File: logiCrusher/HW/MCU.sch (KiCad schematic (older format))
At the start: 13 parts, among them J2 Conn_02x05_Odd_Even, J5 Conn_01x10, J6 Conn_01x10, SW1 SW_Push, U4 STM32F373CCTx

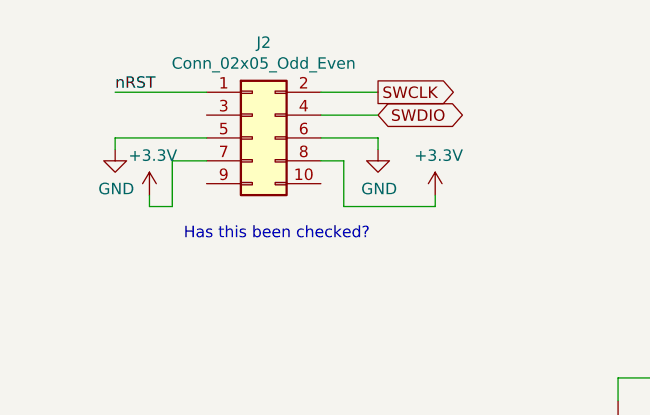
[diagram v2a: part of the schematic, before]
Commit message: Worked on the layout for the logicrusher
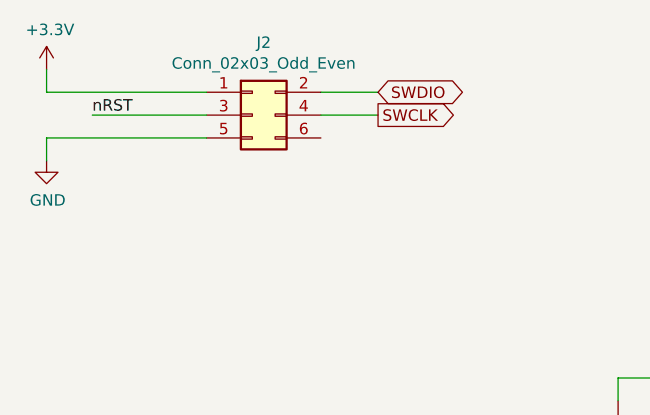
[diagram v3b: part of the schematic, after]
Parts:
- removed J2: Conn_02x05_Odd_Even, symbol Connector_Generic:Conn_02x05_Odd_Even
- added J2: Conn_02x03_Odd_Even, Connector_PinHeader_2.54mm:PinHeader_2x03_P2.54mm_Vertical, symbol Connector_Generic:Conn_02x03_Odd_Even
- J5, J6: footprint (none) -> Connector_PinHeader_2.54mm:PinHeader_1x10_P2.54mm_Vertical
- SW1: footprint (none) -> Button_Switch_THT:SW_Tactile_Straight_KSL0Axx1LFTR
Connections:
- net +3V3: now also J2.1 (Pin_1)
- net GND: now also J2.5 (Pin_5)
- net SWCLK: now also J2.4 (Pin_4)
- net SWDIO: now also J2.2 (Pin_2)
- net nRST: now also J2.3 (Pin_3)
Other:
- note removed: "Has this been checked?"
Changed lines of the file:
@@
 F 0 "SW1" V 3396 2802 50  0000 R CNN
 F 1 "SW_Push" V 3305 2802 50  0000 R CNN
-F 2 "" H 3350 3050 50  0001 C CNN
+F 2 "Button_Switch_THT:SW_Tactile_Straight_KSL0Axx1LFTR" H 3350 3050 50  0001 C CNN
 F 3 "" H 3350 3050 50  0001 C CNN
 	1    3350 2850
@@
 F 0 "J5" H 7830 4642 50  0000 L CNN
 F 1 "Conn_01x10" H 7830 4551 50  0000 L CNN
-F 2 "" H 7750 4650 50  0001 C CNN
+F 2 "Connector_PinHeader_2.54mm:PinHeader_1x10_P2.54mm_Vertical" H 7750 4650 50  0001 C CNN
 F 3 "~" H 7750 4650 50  0001 C CNN
 	1    7750 4650
@@
 F 0 "J6" V 8400 2450 50  0000 L CNN
 F 1 "Conn_01x10" V 8500 2450 50  0000 L CNN
-F 2 "" H 8300 2950 50  0001 C CNN
+F 2 "Connector_PinHeader_2.54mm:PinHeader_1x10_P2.54mm_Vertical" H 8300 2950 50  0001 C CNN
 F 3 "~" H 8300 2950 50  0001 C CNN
 	1    8300 2950
@@
 Text Label 6850 2850 0    50   ~ 0
 ADC3
-Text GLabel 2300 1300 2    50   Output ~ 0
+Text GLabel 2300 1400 2    50   Output ~ 0
 SWCLK
-Text GLabel 2300 1400 2    50   BiDi ~ 0
+Text GLabel 2300 1300 2    50   BiDi ~ 0
 SWDIO
-Text Label 1150 1300 0    50   ~ 0
+Text Label 1050 1400 0    50   ~ 0
 nRST
-$Comp
-L Connector_Generic:Conn_02x05_Odd_Even J?
-U 1 1 5CBA4E93
-P 1750 1500
-AR Path="/5CBA4E93" Ref="J?"  Part="1"
-AR Path="/5CB08311/5CBA4E93" Ref="J2"  Part="1"
-F 0 "J2" H 1800 1917 50  0000 C CNN
-F 1 "Conn_02x05_Odd_Even" H 1800 1826 50  0000 C CNN
-F 2 "" H 1750 1500 50  0001 C CNN
-F 3 "~" H 1750 1500 50  0001 C CNN
-	1    1750 1500
-	1    0    0    -1
-$EndComp
-Wire Wire Line
-	1150 1300 1550 1300
-Wire Wire Line
-	1550 1500 1150 1500
-Wire Wire Line
-	1150 1500 1150 1550
-$Comp
-L power:GND #PWR?
-U 1 1 5CBA4E9D
-P 1150 1550
-AR Path="/5CBA4E9D" Ref="#PWR?"  Part="1"
-AR Path="/5CB08311/5CBA4E9D" Ref="#PWR019"  Part="1"
-F 0 "#PWR019" H 1150 1300 50  0001 C CNN
-F 1 "GND" H 1155 1377 50  0000 C CNN
-F 2 "" H 1150 1550 50  0001 C CNN
-F 3 "" H 1150 1550 50  0001 C CNN
-	1    1150 1550
-	1    0    0    -1
-$EndComp
-$Comp
-L power:GND #PWR?
-U 1 1 5CBA4EA3
-P 2300 1550
-AR Path="/5CBA4EA3" Ref="#PWR?"  Part="1"
-AR Path="/5CB08311/5CBA4EA3" Ref="#PWR022"  Part="1"
-F 0 "#PWR022" H 2300 1300 50  0001 C CNN
-F 1 "GND" H 2305 1377 50  0000 C CNN
-F 2 "" H 2300 1550 50  0001 C CNN
-F 3 "" H 2300 1550 50  0001 C CNN
-	1    2300 1550
-	1    0    0    -1
-$EndComp
+Wire Wire Line
+	850  1300 1550 1300
 Wire Wire Line
 	2050 1300 2300 1300
 Wire Wire Line
 	2050 1400 2300 1400
-Wire Wire Line
-	2050 1500 2300 1500
-Wire Wire Line
-	2300 1500 2300 1550
-$Comp
-L power:+3.3V #PWR?
-U 1 1 5CBA4EAD
-P 1300 1750
-AR Path="/5CBA4EAD" Ref="#PWR?"  Part="1"
-AR Path="/5CB08311/5CBA4EAD" Ref="#PWR021"  Part="1"
-F 0 "#PWR021" H 1300 1600 50  0001 C CNN
-F 1 "+3.3V" H 1315 1923 50  0000 C CNN
-F 2 "" H 1300 1750 50  0001 C CNN
-F 3 "" H 1300 1750 50  0001 C CNN
-	1    1300 1750
-	1    0    0    -1
-$EndComp
-Wire Wire Line
-	1300 1750 1300 1800
-Wire Wire Line
-	1300 1800 1400 1800
-Wire Wire Line
-	1400 1800 1400 1600
-Wire Wire Line
-	1400 1600 1550 1600
-Wire Wire Line
-	2050 1600 2150 1600
-Wire Wire Line
-	2150 1600 2150 1800
-Wire Wire Line
-	2150 1800 2550 1800
-Wire Wire Line
-	2550 1800 2550 1750
-$Comp
-L power:+3.3V #PWR?
-U 1 1 5CBA4EBB
-P 2550 1750
-AR Path="/5CBA4EBB" Ref="#PWR?"  Part="1"
-AR Path="/5CB08311/5CBA4EBB" Ref="#PWR023"  Part="1"
-F 0 "#PWR023" H 2550 1600 50  0001 C CNN
-F 1 "+3.3V" H 2565 1923 50  0000 C CNN
-F 2 "" H 2550 1750 50  0001 C CNN
-F 3 "" H 2550 1750 50  0001 C CNN
-	1    2550 1750
-	1    0    0    -1
-$EndComp
 Text HLabel 6850 4350 2    50   Input ~ 0
 Vin
@@
 Wire Wire Line
 	7550 2400 7550 2850
-Text Notes 1450 1950 0    50   ~ 0
-Has this been checked?
 Wire Wire Line
 	6650 2550 7250 2550
@@
 Wire Wire Line
 	3900 3300 4450 3300
+$Comp
+L power:+3.3V #PWR?
+U 1 1 5CC2437C
+P 850 1200
+AR Path="/5CC2437C" Ref="#PWR?"  Part="1"
+AR Path="/5CB08311/5CC2437C" Ref="#PWR0103"  Part="1"
+F 0 "#PWR0103" H 850 1050 50  0001 C CNN
+F 1 "+3.3V" H 865 1373 50  0000 C CNN
+F 2 "" H 850 1200 50  0001 C CNN
+F 3 "" H 850 1200 50  0001 C CNN
+	1    850  1200
+	1    0    0    -1
+$EndComp
+Wire Wire Line
+	1050 1400 1550 1400
+Wire Wire Line
+	1550 1500 850  1500
+Wire Wire Line
+	850  1500 850  1600
+$Comp
+L power:GND #PWR?
+U 1 1 5CC2EAFE
+P 850 1600
+AR Path="/5CC2EAFE" Ref="#PWR?"  Part="1"
+AR Path="/5CB08311/5CC2EAFE" Ref="#PWR0104"  Part="1"
+F 0 "#PWR0104" H 850 1350 50  0001 C CNN
+F 1 "GND" H 855 1427 50  0000 C CNN
+F 2 "" H 850 1600 50  0001 C CNN
+F 3 "" H 850 1600 50  0001 C CNN
+	1    850  1600
+	1    0    0    -1
+$EndComp
+Wire Wire Line
+	850  1300 850  1200
+$Comp
+L Connector_Generic:Conn_02x03_Odd_Even J2
+U 1 1 5CC38546
+P 1750 1400
+F 0 "J2" H 1800 1717 50  0000 C CNN
+F 1 "Conn_02x03_Odd_Even" H 1800 1626 50  0000 C CNN
+F 2 "Connector_PinHeader_2.54mm:PinHeader_2x03_P2.54mm_Vertical" H 1750 1400 50  0001 C CNN
+F 3 "~" H 1750 1400 50  0001 C CNN
+	1    1750 1400
+	1    0    0    -1
+$EndComp
 $EndSCHEMATC

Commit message: Spend a lot of time working on the logicCrusher HW
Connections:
- net D0: now reaches J5.1 (Pin_1), U4.18 (PB0)
- net D1: now reaches J5.2 (Pin_2), U4.19 (PB1)
- net D2: now reaches J5.3 (Pin_3), U4.39 (PB3)
- net D3: now reaches J5.4 (Pin_4), U4.40 (PB4)
- net D4: now reaches J5.5 (Pin_5), U4.41 (PB5)
- net D5: now reaches J5.6 (Pin_6), U4.42 (PB6)
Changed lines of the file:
@@
 $EndComp
 Wire Wire Line
-	6650 4450 7550 4450
-Wire Wire Line
-	6650 4550 7550 4550
-Wire Wire Line
-	6650 4650 7550 4650
-Wire Wire Line
-	7550 4750 6650 4750
+	6650 4450 7400 4450
+Wire Wire Line
+	6650 4550 7500 4550
+Wire Wire Line
+	6650 4650 7050 4650
+Wire Wire Line
+	7550 4750 7150 4750
 Wire Wire Line
 	6650 4850 7550 4850
@@
 	7100 4250 7100 4350
 Wire Wire Line
-	7100 4350 7550 4350
+	7100 4350 7300 4350
 Wire Wire Line
 	6650 4150 7200 4150
 Wire Wire Line
 	7200 4150 7200 4250
-Wire Wire Line
-	7200 4250 7550 4250
 Wire Wire Line
 	7550 5150 6650 5150
@@
 	1    0    0    -1
 $EndComp
+Text HLabel 7200 4100 1    50   Output ~ 0
+D0
+Text HLabel 7300 4100 1    50   Output ~ 0
+D1
+Text HLabel 7400 4100 1    50   Output ~ 0
+D2
+Text HLabel 7500 4100 1    50   Output ~ 0
+D3
+Wire Wire Line
+	7200 4100 7200 4150
+Wire Wire Line
+	7200 4250 7550 4250
+Wire Wire Line
+	7300 4100 7300 4350
+Connection ~ 7300 4350
+Wire Wire Line
+	7300 4350 7550 4350
+Wire Wire Line
+	7400 4100 7400 4450
+Connection ~ 7400 4450
+Wire Wire Line
+	7400 4450 7550 4450
+Connection ~ 7500 4550
+Wire Wire Line
+	7500 4550 7550 4550
+Text HLabel 7050 5250 3    50   Input ~ 0
+D4
+Text HLabel 7150 5250 3    50   Input ~ 0
+D5
+Wire Wire Line
+	7050 5250 7050 4650
+Connection ~ 7050 4650
+Wire Wire Line
+	7050 4650 7550 4650
+Wire Wire Line
+	7150 5250 7150 4750
+Connection ~ 7150 4750
+Wire Wire Line
+	7150 4750 6650 4750
+Connection ~ 7200 4150
+Wire Wire Line
+	7500 4100 7500 4550
 $EndSCHEMATC

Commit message: Made fabrication files
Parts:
- removed SW1: SW_Push, Button_Switch_THT:SW_Tactile_Straight_KSL0Axx1LFTR, symbol Switch:SW_Push
- added SW1: TL1105SPF250Q, Eurocad:TL1105SPF250Q, symbol eurocad:TL1105SPF250Q
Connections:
- net GND: now also SW1.3
- net nRST: now also SW1.1, SW1.2
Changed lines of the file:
@@
 Text GLabel 6800 3950 2    50   BiDi ~ 0
 SWDIO
-$Comp
-L Switch:SW_Push SW?
-U 1 1 5CB1AF99
-P 3350 2850
-AR Path="/5CB1AF99" Ref="SW?"  Part="1"
-AR Path="/5CB08311/5CB1AF99" Ref="SW1"  Part="1"
-F 0 "SW1" V 3396 2802 50  0000 R CNN
-F 1 "SW_Push" V 3305 2802 50  0000 R CNN
-F 2 "Button_Switch_THT:SW_Tactile_Straight_KSL0Axx1LFTR" H 3350 3050 50  0001 C CNN
-F 3 "" H 3350 3050 50  0001 C CNN
-	1    3350 2850
-	0    -1   -1   0
-$EndComp
-Wire Wire Line
-	3350 2650 3350 2550
 Wire Wire Line
 	3350 3050 3350 3100
@@
 Wire Wire Line
 	3800 3050 3350 3050
-Connection ~ 3350 3050
 Wire Wire Line
 	5250 2750 4750 2750
@@
 	0    1    1    0
 $EndComp
-Wire Wire Line
-	3350 2550 3800 2550
 Connection ~ 3800 2550
 Wire Wire Line
@@
 Wire Wire Line
 	7500 4100 7500 4550
+$Comp
+L eurocad:TL1105SPF250Q SW1
+U 1 1 5CC32E6D
+P 2500 2900
+F 0 "SW1" V 2454 3228 50  0000 L CNN
+F 1 "TL1105SPF250Q" V 2545 3228 50  0000 L CNN
+F 2 "Eurocad:TL1105SPF250Q" H 2500 2900 50  0001 C CNN
+F 3 "" H 2500 2900 50  0000 C CNN
+	1    2500 2900
+	0    1    1    0
+$EndComp
+Wire Wire Line
+	2300 2600 2300 2550
+Wire Wire Line
+	2300 2550 2700 2550
+Wire Wire Line
+	2700 2600 2700 2550
+Connection ~ 2700 2550
+Wire Wire Line
+	2700 2550 3800 2550
+Wire Wire Line
+	2300 3200 2300 3300
+Wire Wire Line
+	2300 3300 2500 3300
+Wire Wire Line
+	2700 3300 2700 3200
+$Comp
+L power:GND #PWR?
+U 1 1 5CC4367C
+P 2500 3400
+AR Path="/5CC4367C" Ref="#PWR?"  Part="1"
+AR Path="/5CB08311/5CC4367C" Ref="#PWR0105"  Part="1"
+F 0 "#PWR0105" H 2500 3150 50  0001 C CNN
+F 1 "GND" H 2505 3227 50  0000 C CNN
+F 2 "" H 2500 3400 50  0001 C CNN
+F 3 "" H 2500 3400 50  0001 C CNN
+	1    2500 3400
+	1    0    0    -1
+$EndComp
+Wire Wire Line
+	2500 3400 2500 3300
+Connection ~ 2500 3300
+Wire Wire Line
+	2500 3300 2700 3300
 $EndSCHEMATC
